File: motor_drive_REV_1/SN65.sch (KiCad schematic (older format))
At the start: 15 parts, among them U6 SN65LBC176QDRQ1

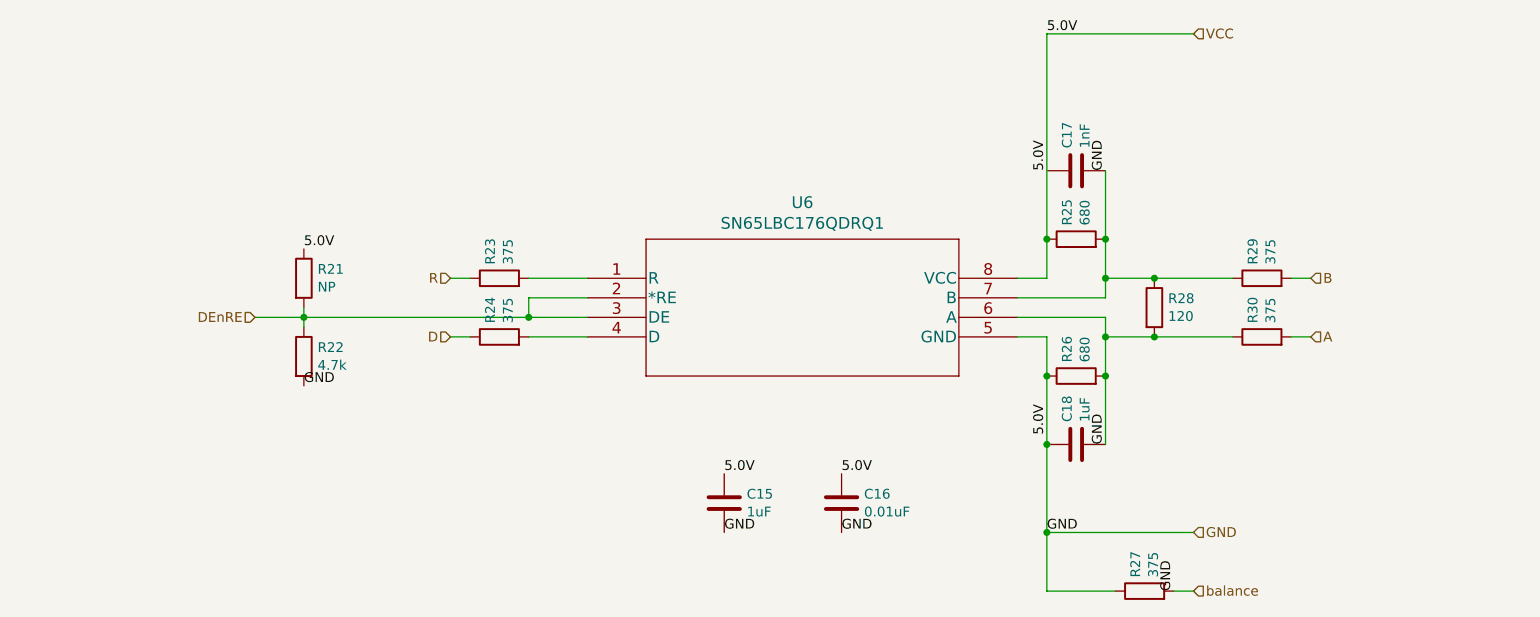
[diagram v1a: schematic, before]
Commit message: working on adding thermistors but encountered too many hierarchicaly copies bug
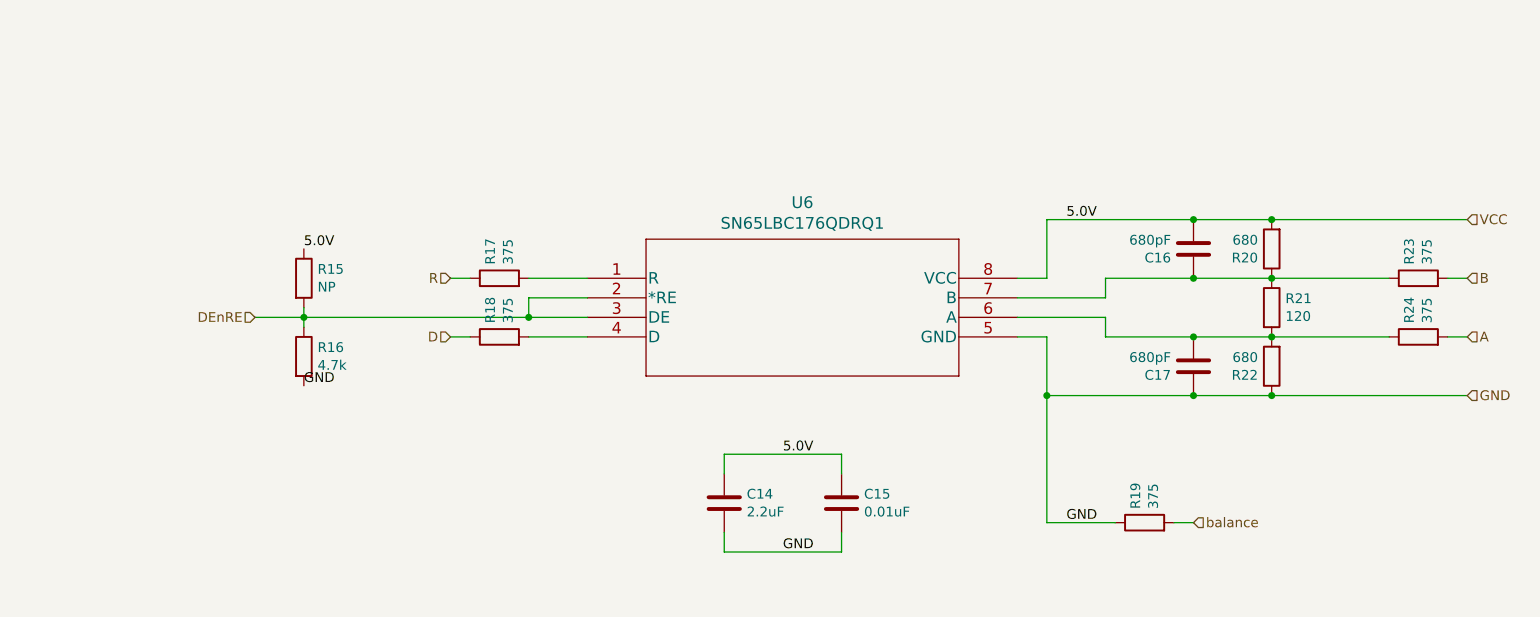
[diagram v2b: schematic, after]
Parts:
- removed C17: 1nF, motor_drive_footprints:C_0603_1608Metric, symbol motor_drive:C
- removed R25: 680, motor_drive_footprints:C_0603_1608Metric, symbol motor_drive:R
- added C16: 680pF, motor_drive_footprints:C_0603_1608Metric, symbol motor_drive:C
- added R20: 680, motor_drive_footprints:C_0603_1608Metric, symbol motor_drive:R
- C14: renamed from C15; value 1uF -> 2.2uF
- C17: renamed from C18; value 1uF -> 680pF
- renumbered C16 to C15, R21 to R15, R22 to R16, R23 to R17, R24 to R18, R27 to R19, R28 to R21, R26 to R22, R29 to R23, R30 to R24
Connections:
- net GND: no longer C14.1, C15.1, C17.2, R15.1, R19.2, R21.1, R21.2, R22.2, R23.1, R24.1, U6.6 (A), U6.7 (B), U6.8 (VCC)
- new net: C17.2, R21.2, R22.2, R24.1, U6.6 (A)
- new net: C16.1, R20.1, R21.1, R23.1, U6.7 (B)
- new net VCC: C14.1, C15.1, C16.2, R15.1, R20.2, U6.8 (VCC)
- new net balance: R19.2
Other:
- moved on the sheet: C17, R19, R21, R22, R23, R24
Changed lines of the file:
@@
 Comment4 ""
 $EndDescr
-Text HLabel 7900 4800 2    50   Input ~ 0
+Text HLabel 9300 4100 2    50   Input ~ 0
 GND
 Wire Wire Line
 	7000 3800 7150 3800
-Text HLabel 7900 2250 2    50   Input ~ 0
+Text HLabel 9300 3200 2    50   Input ~ 0
 VCC
 Wire Wire Line
@@
 Wire Wire Line
 	4500 3600 4500 3700
-Wire Wire Line
-	7150 4800 7900 4800
-Wire Wire Line
-	7900 2250 7150 2250
-$Comp
-L motor_drive:R R21
+$Comp
+L motor_drive:R R15
 U 1 1 5E39658B
 P 3350 3500
-F 0 "R21" H 3420 3546 50  0000 L CNN
+F 0 "R15" H 3420 3546 50  0000 L CNN
 F 1 "NP" H 3420 3455 50  0000 L CNN
 F 2 "motor_drive_footprints:C_0603_1608Metric" V 3280 3500 50  0001 C CNN
@@
 	3350 3700 3350 3750
 $Comp
-L motor_drive:C C15
+L motor_drive:C C14
 U 1 1 5E39B417
 P 5500 4650
-F 0 "C15" H 5615 4696 50  0000 L CNN
-F 1 "1uF" H 5615 4605 50  0000 L CNN
+F 0 "C14" H 5615 4696 50  0000 L CNN
+F 1 "2.2uF" H 5615 4605 50  0000 L CNN
 F 2 "motor_drive_footprints:C_0603_1608Metric" H 5538 4500 50  0001 C CNN
 F 3 "~" H 5500 4650 50  0001 C CNN
@@
 	1    0    0    -1
 $EndComp
-Text Label 5500 4500 0    50   ~ 0
+Text Label 5800 4400 0    50   ~ 0
 5.0V
-Text Label 5500 4800 0    50   ~ 0
-GND
-$Comp
-L motor_drive:R R22
+$Comp
+L motor_drive:R R16
 U 1 1 5E39AB4E
 P 3350 3900
-F 0 "R22" H 3420 3946 50  0000 L CNN
+F 0 "R16" H 3420 3946 50  0000 L CNN
 F 1 "4.7k" H 3420 3855 50  0000 L CNN
 F 2 "motor_drive_footprints:C_0603_1608Metric" V 3280 3900 50  0001 C CNN
@@
 	1    0    0    -1
 $EndComp
-Text Label 7150 2250 0    50   ~ 0
+Text Label 7250 3200 0    50   ~ 0
 5.0V
-Text Label 7150 4800 0    50   ~ 0
+Text Label 7250 4750 0    50   ~ 0
 GND
 Text Label 3350 3350 0    50   ~ 0
@@
 GND
 $Comp
-L motor_drive:R R23
+L motor_drive:R R17
 U 1 1 5E3A24BE
 P 4350 3500
-F 0 "R23" H 4420 3546 50  0000 L CNN
+F 0 "R17" H 4420 3546 50  0000 L CNN
 F 1 "375" H 4420 3455 50  0000 L CNN
 F 2 "motor_drive_footprints:C_0603_1608Metric" V 4280 3500 50  0001 C CNN
@@
 $EndComp
 $Comp
-L motor_drive:R R24
+L motor_drive:R R18
 U 1 1 5E3A2A5B
 P 4350 3800
-F 0 "R24" H 4420 3846 50  0000 L CNN
+F 0 "R18" H 4420 3846 50  0000 L CNN
 F 1 "375" H 4420 3755 50  0000 L CNN
 F 2 "motor_drive_footprints:C_0603_1608Metric" V 4280 3800 50  0001 C CNN
@@
 	4500 3800 4800 3800
 $Comp
-L motor_drive:R R27
+L motor_drive:R R19
 U 1 1 5E33ED83
-P 7650 5100
-F 0 "R27" H 7720 5146 50  0000 L CNN
-F 1 "375" H 7720 5055 50  0000 L CNN
-F 2 "motor_drive_footprints:C_0603_1608Metric" V 7580 5100 50  0001 C CNN
-F 3 "~" H 7650 5100 50  0001 C CNN
-	1    7650 5100
-	0    -1   -1   0
-$EndComp
-Text Label 7800 5100 1    50   ~ 0
-GND
-Text HLabel 7900 5100 2    50   Input ~ 0
+P 7650 4750
+F 0 "R19" H 7720 4796 50  0000 L CNN
+F 1 "375" H 7720 4705 50  0000 L CNN
+F 2 "motor_drive_footprints:C_0603_1608Metric" V 7580 4750 50  0001 C CNN
+F 3 "~" H 7650 4750 50  0001 C CNN
+	1    7650 4750
+	0    -1   -1   0
+$EndComp
+Text HLabel 7900 4750 2    50   Input ~ 0
 balance
 Wire Wire Line
-	7800 5100 7900 5100
-Wire Wire Line
-	7500 5100 7150 5100
-Wire Wire Line
-	7150 5100 7150 4800
-Connection ~ 7150 4800
-$Comp
-L motor_drive:R R28
+	7800 4750 7900 4750
+Wire Wire Line
+	7500 4750 7150 4750
+$Comp
+L motor_drive:R R21
 U 1 1 5E390D6F
-P 7700 3650
-F 0 "R28" H 7770 3696 50  0000 L CNN
-F 1 "120" H 7770 3605 50  0000 L CNN
-F 2 "motor_drive_footprints:C_0603_1608Metric" V 7630 3650 50  0001 C CNN
-F 3 "~" H 7700 3650 50  0001 C CNN
-	1    7700 3650
+P 8300 3650
+F 0 "R21" H 8370 3696 50  0000 L CNN
+F 1 "120" H 8370 3605 50  0000 L CNN
+F 2 "motor_drive_footprints:C_0603_1608Metric" V 8230 3650 50  0001 C CNN
+F 3 "~" H 8300 3650 50  0001 C CNN
+	1    8300 3650
 	1    0    0    -1
 $EndComp
 Wire Wire Line
 	7450 3700 7450 3800
-Text HLabel 8500 3500 2    50   Input ~ 0
+Text HLabel 9300 3500 2    50   Input ~ 0
 B
-Text HLabel 8500 3800 2    50   Input ~ 0
+Text HLabel 9300 3800 2    50   Input ~ 0
 A
-Wire Wire Line
-	7700 3500 8100 3500
-Connection ~ 7700 3800
-Wire Wire Line
-	7700 3800 8100 3800
-Wire Wire Line
-	7450 3800 7700 3800
-$Comp
-L motor_drive:R R26
+$Comp
+L motor_drive:R R22
 U 1 1 5E37C57B
-P 7300 4000
-F 0 "R26" H 7370 4046 50  0000 L CNN
-F 1 "680" H 7370 3955 50  0000 L CNN
-F 2 "motor_drive_footprints:C_0603_1608Metric" V 7230 4000 50  0001 C CNN
-F 3 "~" H 7300 4000 50  0001 C CNN
-	1    7300 4000
-	0    -1   -1   0
-$EndComp
-$Comp
-L motor_drive:R R25
-U 1 1 5E37CBBC
-P 7300 3300
-F 0 "R25" H 7370 3346 50  0000 L CNN
-F 1 "680" H 7370 3255 50  0000 L CNN
-F 2 "motor_drive_footprints:C_0603_1608Metric" V 7230 3300 50  0001 C CNN
-F 3 "~" H 7300 3300 50  0001 C CNN
-	1    7300 3300
-	0    -1   -1   0
+P 8300 3950
+F 0 "R22" H 8370 3996 50  0000 L CNN
+F 1 "680" H 8370 3905 50  0000 L CNN
+F 2 "motor_drive_footprints:C_0603_1608Metric" V 8230 3950 50  0001 C CNN
+F 3 "~" H 8300 3950 50  0001 C CNN
+	1    8300 3950
+	-1   0    0    1
 $EndComp
 Wire Wire Line
@@
 	7000 3700 7450 3700
 $Comp
-L motor_drive:R R29
+L motor_drive:R R23
 U 1 1 5E37EDA8
-P 8250 3500
-F 0 "R29" H 8320 3546 50  0000 L CNN
-F 1 "375" H 8320 3455 50  0000 L CNN
-F 2 "motor_drive_footprints:C_0603_1608Metric" V 8180 3500 50  0001 C CNN
-F 3 "~" H 8250 3500 50  0001 C CNN
-	1    8250 3500
-	0    -1   -1   0
-$EndComp
-$Comp
-L motor_drive:R R30
+P 9050 3500
+F 0 "R23" H 9120 3546 50  0000 L CNN
+F 1 "375" H 9120 3455 50  0000 L CNN
+F 2 "motor_drive_footprints:C_0603_1608Metric" V 8980 3500 50  0001 C CNN
+F 3 "~" H 9050 3500 50  0001 C CNN
+	1    9050 3500
+	0    -1   -1   0
+$EndComp
+$Comp
+L motor_drive:R R24
 U 1 1 5E37F275
-P 8250 3800
-F 0 "R30" H 8320 3846 50  0000 L CNN
-F 1 "375" H 8320 3755 50  0000 L CNN
-F 2 "motor_drive_footprints:C_0603_1608Metric" V 8180 3800 50  0001 C CNN
-F 3 "~" H 8250 3800 50  0001 C CNN
-	1    8250 3800
-	0    -1   -1   0
-$EndComp
-Wire Wire Line
-	8400 3500 8500 3500
-Wire Wire Line
-	8400 3800 8500 3800
-Wire Wire Line
-	7150 3800 7150 4000
-Wire Wire Line
-	7150 2250 7150 3300
-Connection ~ 7150 4000
-Wire Wire Line
-	7150 4000 7150 4350
-Connection ~ 7150 3300
-Wire Wire Line
-	7150 3300 7150 3500
-$Comp
-L motor_drive:C C18
+P 9050 3800
+F 0 "R24" H 9120 3846 50  0000 L CNN
+F 1 "375" H 9120 3755 50  0000 L CNN
+F 2 "motor_drive_footprints:C_0603_1608Metric" V 8980 3800 50  0001 C CNN
+F 3 "~" H 9050 3800 50  0001 C CNN
+	1    9050 3800
+	0    -1   -1   0
+$EndComp
+Wire Wire Line
+	9200 3500 9300 3500
+Wire Wire Line
+	9200 3800 9300 3800
+$Comp
+L motor_drive:C C17
 U 1 1 5E386871
-P 7300 4350
-F 0 "C18" H 7415 4396 50  0000 L CNN
-F 1 "1uF" H 7415 4305 50  0000 L CNN
-F 2 "motor_drive_footprints:C_0603_1608Metric" H 7338 4200 50  0001 C CNN
-F 3 "~" H 7300 4350 50  0001 C CNN
-	1    7300 4350
-	0    -1   -1   0
-$EndComp
-Text Label 7150 4300 1    50   ~ 0
-5.0V
-Text Label 7450 4350 1    50   ~ 0
-GND
-$Comp
-L motor_drive:C C17
-U 1 1 5E387278
-P 7300 2950
-F 0 "C17" H 7415 2996 50  0000 L CNN
-F 1 "1nF" H 7415 2905 50  0000 L CNN
-F 2 "motor_drive_footprints:C_0603_1608Metric" H 7338 2800 50  0001 C CNN
-F 3 "~" H 7300 2950 50  0001 C CNN
-	1    7300 2950
-	0    -1   -1   0
-$EndComp
-Text Label 7150 2950 1    50   ~ 0
-5.0V
-Text Label 7450 2950 1    50   ~ 0
-GND
-Wire Wire Line
-	7450 3800 7450 4000
-Connection ~ 7450 3800
+P 7900 3950
+F 0 "C17" H 8015 3996 50  0000 L CNN
+F 1 "680pF" H 8015 3905 50  0000 L CNN
+F 2 "motor_drive_footprints:C_0603_1608Metric" H 7938 3800 50  0001 C CNN
+F 3 "~" H 7900 3950 50  0001 C CNN
+	1    7900 3950
+	-1   0    0    1
+$EndComp
 Wire Wire Line
 	7450 3600 7450 3500
-Wire Wire Line
-	7450 3300 7450 2950
-Connection ~ 7450 3300
-Connection ~ 7150 4350
-Wire Wire Line
-	7150 4350 7150 4800
-Wire Wire Line
-	7450 4000 7450 4350
-Connection ~ 7450 4000
-Wire Wire Line
-	7700 3500 7450 3500
-Connection ~ 7700 3500
-Connection ~ 7450 3500
-Wire Wire Line
-	7450 3500 7450 3300
-$Comp
-L motor_drive:C C16
+$Comp
+L motor_drive:C C15
 U 1 1 5E3AD083
 P 6100 4650
-F 0 "C16" H 6215 4696 50  0000 L CNN
+F 0 "C15" H 6215 4696 50  0000 L CNN
 F 1 "0.01uF" H 6215 4605 50  0000 L CNN
 F 2 "motor_drive_footprints:C_0603_1608Metric" H 6138 4500 50  0001 C CNN
@@
 	1    0    0    -1
 $EndComp
-Text Label 6100 4500 0    50   ~ 0
-5.0V
-Text Label 6100 4800 0    50   ~ 0
+Connection ~ 8300 3500
+Wire Wire Line
+	8300 3500 8900 3500
+Connection ~ 8300 3800
+Wire Wire Line
+	8300 3800 8900 3800
+Wire Wire Line
+	7450 3800 7900 3800
+Connection ~ 7900 3800
+Wire Wire Line
+	7900 3800 8300 3800
+$Comp
+L motor_drive:R R20
+U 1 1 5E5DB1A4
+P 8300 3350
+F 0 "R20" H 8370 3396 50  0000 L CNN
+F 1 "680" H 8370 3305 50  0000 L CNN
+F 2 "motor_drive_footprints:C_0603_1608Metric" V 8230 3350 50  0001 C CNN
+F 3 "~" H 8300 3350 50  0001 C CNN
+	1    8300 3350
+	-1   0    0    1
+$EndComp
+$Comp
+L motor_drive:C C16
+U 1 1 5E5DB1AA
+P 7900 3350
+F 0 "C16" H 8015 3396 50  0000 L CNN
+F 1 "680pF" H 8015 3305 50  0000 L CNN
+F 2 "motor_drive_footprints:C_0603_1608Metric" H 7938 3200 50  0001 C CNN
+F 3 "~" H 7900 3350 50  0001 C CNN
+	1    7900 3350
+	-1   0    0    1
+$EndComp
+Wire Wire Line
+	7150 3800 7150 4100
+Wire Wire Line
+	8300 4100 9300 4100
+Wire Wire Line
+	8300 4100 7900 4100
+Connection ~ 8300 4100
+Wire Wire Line
+	7900 4100 7150 4100
+Connection ~ 7900 4100
+Wire Wire Line
+	8300 3200 9300 3200
+Wire Wire Line
+	8300 3200 7900 3200
+Connection ~ 8300 3200
+Wire Wire Line
+	7900 3200 7150 3200
+Connection ~ 7900 3200
+Wire Wire Line
+	7150 3200 7150 3500
+Wire Wire Line
+	8300 3500 7900 3500
+Wire Wire Line
+	7900 3500 7450 3500
+Connection ~ 7900 3500
+Wire Wire Line
+	7150 4100 7150 4750
+Connection ~ 7150 4100
+Wire Wire Line
+	5500 4500 5500 4400
+Wire Wire Line
+	5500 4400 6100 4400
+Wire Wire Line
+	6100 4400 6100 4500
+Wire Wire Line
+	6100 4900 6100 4800
+Wire Wire Line
+	6100 4900 5500 4900
+Wire Wire Line
+	5500 4900 5500 4800
+Text Label 5800 4900 0    50   ~ 0
 GND
 $EndSCHEMATC

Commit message: started layout
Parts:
- renumbered C14 to C23, C15 to C24, C16 to C25, C17 to C26, R15 to R13, R16 to R14, R17 to R15, R18 to R16, R19 to R17, R20 to R18, R21 to R19, R22 to R20, R23 to R21, R24 to R22
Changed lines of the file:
@@
 $Descr A4 11693 8268
 encoding utf-8
-Sheet 11 14
+Sheet 11 16
 Title ""
 Date ""
@@
 	4500 3600 4500 3700
 $Comp
-L motor_drive:R R15
+L motor_drive:R R13
 U 1 1 5E39658B
 P 3350 3500
-F 0 "R15" H 3420 3546 50  0000 L CNN
+F 0 "R13" H 3420 3546 50  0000 L CNN
 F 1 "NP" H 3420 3455 50  0000 L CNN
 F 2 "motor_drive_footprints:C_0603_1608Metric" V 3280 3500 50  0001 C CNN
@@
 	3350 3700 3350 3750
 $Comp
-L motor_drive:C C14
+L motor_drive:C C23
 U 1 1 5E39B417
 P 5500 4650
-F 0 "C14" H 5615 4696 50  0000 L CNN
+F 0 "C23" H 5615 4696 50  0000 L CNN
 F 1 "2.2uF" H 5615 4605 50  0000 L CNN
 F 2 "motor_drive_footprints:C_0603_1608Metric" H 5538 4500 50  0001 C CNN
@@
 5.0V
 $Comp
-L motor_drive:R R16
+L motor_drive:R R14
 U 1 1 5E39AB4E
 P 3350 3900
-F 0 "R16" H 3420 3946 50  0000 L CNN
+F 0 "R14" H 3420 3946 50  0000 L CNN
 F 1 "4.7k" H 3420 3855 50  0000 L CNN
 F 2 "motor_drive_footprints:C_0603_1608Metric" V 3280 3900 50  0001 C CNN
@@
 GND
 $Comp
-L motor_drive:R R17
+L motor_drive:R R15
 U 1 1 5E3A24BE
 P 4350 3500
-F 0 "R17" H 4420 3546 50  0000 L CNN
+F 0 "R15" H 4420 3546 50  0000 L CNN
 F 1 "375" H 4420 3455 50  0000 L CNN
 F 2 "motor_drive_footprints:C_0603_1608Metric" V 4280 3500 50  0001 C CNN
@@
 $EndComp
 $Comp
-L motor_drive:R R18
+L motor_drive:R R16
 U 1 1 5E3A2A5B
 P 4350 3800
-F 0 "R18" H 4420 3846 50  0000 L CNN
+F 0 "R16" H 4420 3846 50  0000 L CNN
 F 1 "375" H 4420 3755 50  0000 L CNN
 F 2 "motor_drive_footprints:C_0603_1608Metric" V 4280 3800 50  0001 C CNN
@@
 	4500 3800 4800 3800
 $Comp
-L motor_drive:R R19
+L motor_drive:R R17
 U 1 1 5E33ED83
 P 7650 4750
-F 0 "R19" H 7720 4796 50  0000 L CNN
+F 0 "R17" H 7720 4796 50  0000 L CNN
 F 1 "375" H 7720 4705 50  0000 L CNN
 F 2 "motor_drive_footprints:C_0603_1608Metric" V 7580 4750 50  0001 C CNN
@@
 	7500 4750 7150 4750
 $Comp
-L motor_drive:R R21
+L motor_drive:R R19
 U 1 1 5E390D6F
 P 8300 3650
-F 0 "R21" H 8370 3696 50  0000 L CNN
+F 0 "R19" H 8370 3696 50  0000 L CNN
 F 1 "120" H 8370 3605 50  0000 L CNN
 F 2 "motor_drive_footprints:C_0603_1608Metric" V 8230 3650 50  0001 C CNN
@@
 A
 $Comp
-L motor_drive:R R22
+L motor_drive:R R20
 U 1 1 5E37C57B
 P 8300 3950
-F 0 "R22" H 8370 3996 50  0000 L CNN
+F 0 "R20" H 8370 3996 50  0000 L CNN
 F 1 "680" H 8370 3905 50  0000 L CNN
 F 2 "motor_drive_footprints:C_0603_1608Metric" V 8230 3950 50  0001 C CNN
@@
 	7000 3700 7450 3700
 $Comp
-L motor_drive:R R23
+L motor_drive:R R21
 U 1 1 5E37EDA8
 P 9050 3500
-F 0 "R23" H 9120 3546 50  0000 L CNN
+F 0 "R21" H 9120 3546 50  0000 L CNN
 F 1 "375" H 9120 3455 50  0000 L CNN
 F 2 "motor_drive_footprints:C_0603_1608Metric" V 8980 3500 50  0001 C CNN
@@
 $EndComp
 $Comp
-L motor_drive:R R24
+L motor_drive:R R22
 U 1 1 5E37F275
 P 9050 3800
-F 0 "R24" H 9120 3846 50  0000 L CNN
+F 0 "R22" H 9120 3846 50  0000 L CNN
 F 1 "375" H 9120 3755 50  0000 L CNN
 F 2 "motor_drive_footprints:C_0603_1608Metric" V 8980 3800 50  0001 C CNN
@@
 	9200 3800 9300 3800
 $Comp
-L motor_drive:C C17
+L motor_drive:C C26
 U 1 1 5E386871
 P 7900 3950
-F 0 "C17" H 8015 3996 50  0000 L CNN
+F 0 "C26" H 8015 3996 50  0000 L CNN
 F 1 "680pF" H 8015 3905 50  0000 L CNN
 F 2 "motor_drive_footprints:C_0603_1608Metric" H 7938 3800 50  0001 C CNN
@@
 	7450 3600 7450 3500
 $Comp
-L motor_drive:C C15
+L motor_drive:C C24
 U 1 1 5E3AD083
 P 6100 4650
-F 0 "C15" H 6215 4696 50  0000 L CNN
+F 0 "C24" H 6215 4696 50  0000 L CNN
 F 1 "0.01uF" H 6215 4605 50  0000 L CNN
 F 2 "motor_drive_footprints:C_0603_1608Metric" H 6138 4500 50  0001 C CNN
@@
 	7900 3800 8300 3800
 $Comp
-L motor_drive:R R20
+L motor_drive:R R18
 U 1 1 5E5DB1A4
 P 8300 3350
-F 0 "R20" H 8370 3396 50  0000 L CNN
+F 0 "R18" H 8370 3396 50  0000 L CNN
 F 1 "680" H 8370 3305 50  0000 L CNN
 F 2 "motor_drive_footprints:C_0603_1608Metric" V 8230 3350 50  0001 C CNN
@@
 $EndComp
 $Comp
-L motor_drive:C C16
+L motor_drive:C C25
 U 1 1 5E5DB1AA
 P 7900 3350
-F 0 "C16" H 8015 3396 50  0000 L CNN
+F 0 "C25" H 8015 3396 50  0000 L CNN
 F 1 "680pF" H 8015 3305 50  0000 L CNN
 F 2 "motor_drive_footprints:C_0603_1608Metric" H 7938 3200 50  0001 C CNN
